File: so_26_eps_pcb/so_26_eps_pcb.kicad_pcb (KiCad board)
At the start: 4 copper layers, 90.2 x 95.9 mm, 47 parts, among them J1 Conn_02x12_Odd_Even, J3 Conn_01x02, SW1 SW_SPDT, U1 LM22679TJ-ADJ/NOPB, U2 LM22679TJ-ADJ/NOPB

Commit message: Started the 3V3 reg
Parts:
- moved D1 128.4 mm to (72.5, 88.1), turned to 180 degrees
- moved L1 108.2 mm to (82.7, 94.2)
- moved R3 108.0 mm to (97.8, 77.8), turned to -90 degrees
- moved R7 107.2 mm to (104.4, 81.1), turned to -90 degrees
- moved C13 101.0 mm to (90.4, 95.4), turned to -90 degrees
- moved R5 100.9 mm to (103.4, 77.0), turned to 180 degrees
- moved C17 99.9 mm to (102.6, 85.9), turned to 180 degrees
- moved C15 98.4 mm to (102.6, 88.7), turned to 180 degrees
- moved C11 96.2 mm to (98.0, 95.4), turned to -90 degrees
- moved C10 76.4 mm to (120.4, 78.8)
- moved C7 1.70 mm to (100.1, 78.6), turned to 90 degrees
- moved R8 1.29 mm to (114.0, 55.9)
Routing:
- net Net-(D2-K): track 29.3 -> 3.84 mm
- net REG_+3V3: track 0.00 -> 22.1 mm
- net Net-(U1-FB): track 0.00 -> 10.0 mm
- net Net-(U1-IADJ): track 0.00 -> 8.15 mm
- net Net-(U1-SS): track 0.00 -> 3.51 mm
- net Net-(U2-FB): track 12.0 -> 13.3 mm
- added copper zone on B.Cu, net REG_+3V3

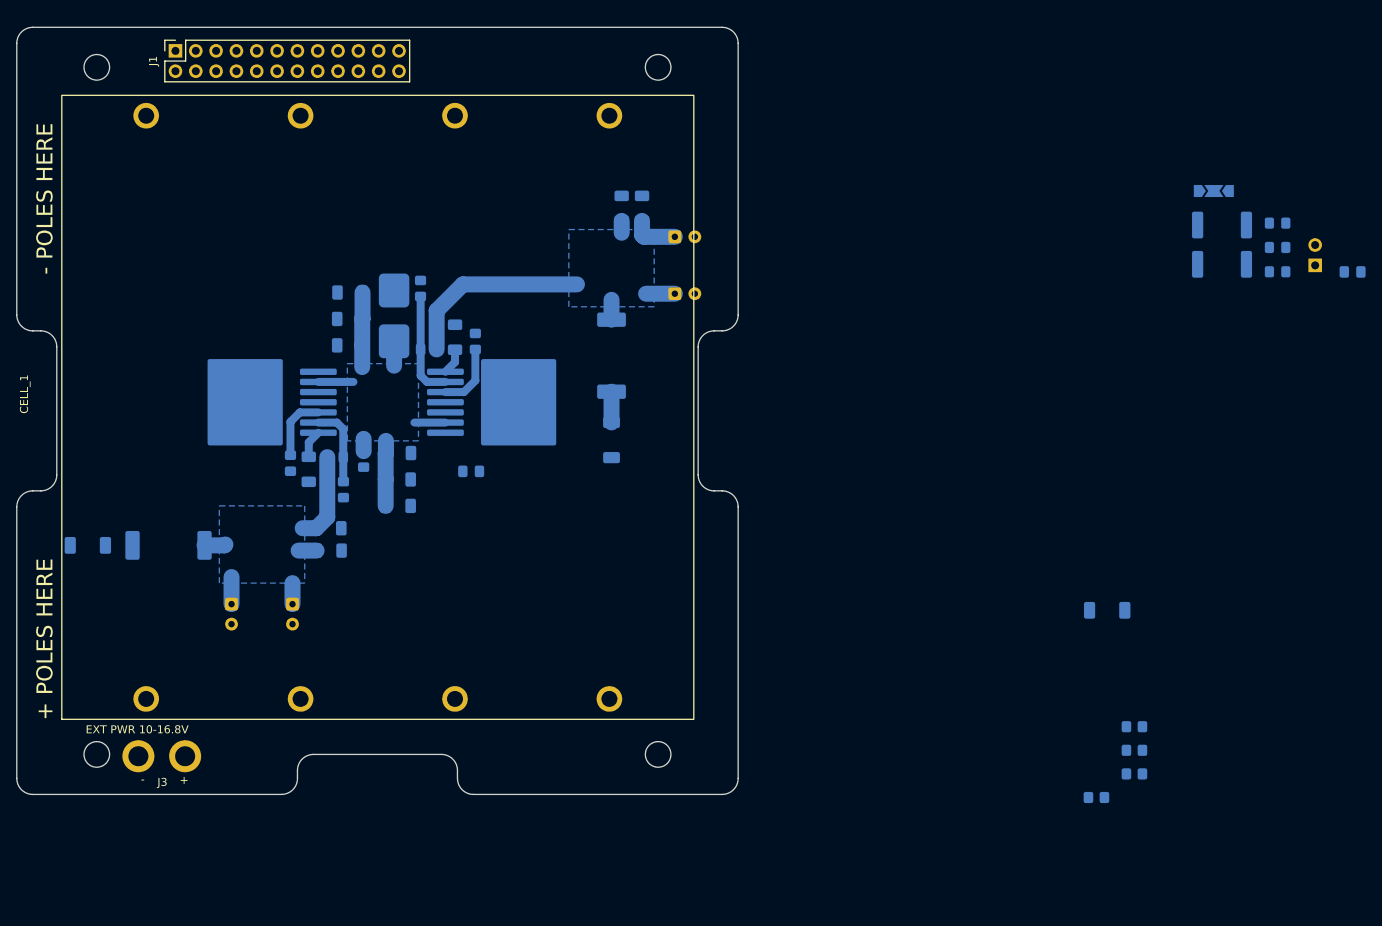
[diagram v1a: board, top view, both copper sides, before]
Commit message: Finished the 3V3 reg
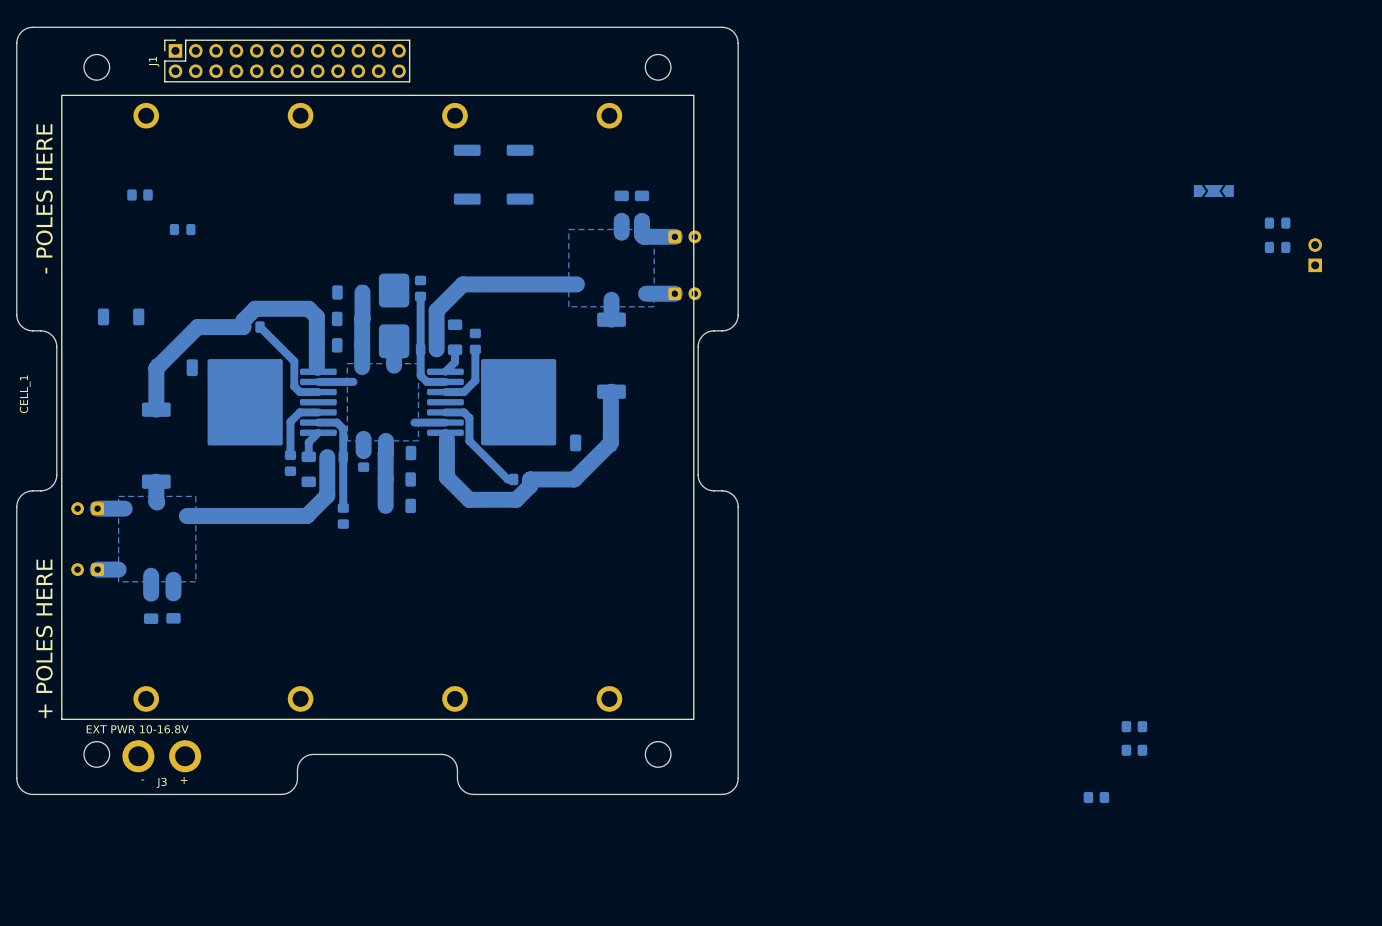
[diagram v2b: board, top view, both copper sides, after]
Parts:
- moved R11 143.8 mm to (79.0, 44.3)
- moved C9 137.8 mm to (92.9, 60.8), turned to 180 degrees
- moved D4 137.0 mm to (84.3, 48.6)
- moved D3 128.6 mm to (76.6, 59.5)
- moved R10 94.6 mm to (119.9, 41.7), turned to 90 degrees
- moved R9 88.5 mm to (126.5, 41.7), turned to 90 degrees
- moved C11 24.7 mm to (73.7, 91.1), turned to 180 degrees
- moved D1 24.7 mm to (83.3, 65.9), turned to 0 degrees
- moved C15 23.3 mm to (80.4, 95.7), turned to 90 degrees
- moved C17 21.7 mm to (83.2, 95.6), turned to 90 degrees
- moved C13 20.6 mm to (73.7, 83.5), turned to 180 degrees
- moved L1 20.0 mm to (74.9, 75.7), turned to -90 degrees
- moved C10 6.43 mm to (126.7, 79.8)
- moved R7 3.30 mm to (104.4, 84.4)
- moved D2 2.31 mm to (135.6, 75.3), turned to 180 degrees
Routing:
- net Net-(D1-K): track 0.00 -> 36.1 mm
- net Net-(D2-K): track 3.84 -> 37.2 mm
- net REG_+3V3: track 22.1 -> 36.0 mm
- net Net-(U2-BOOT): track 0.00 -> 13.7 mm
- net Net-(U1-BOOT): track 0.00 -> 12.5 mm
- net Net-(U1-FB): track 10.0 -> 13.3 mm

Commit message: Uptaded switch footprints
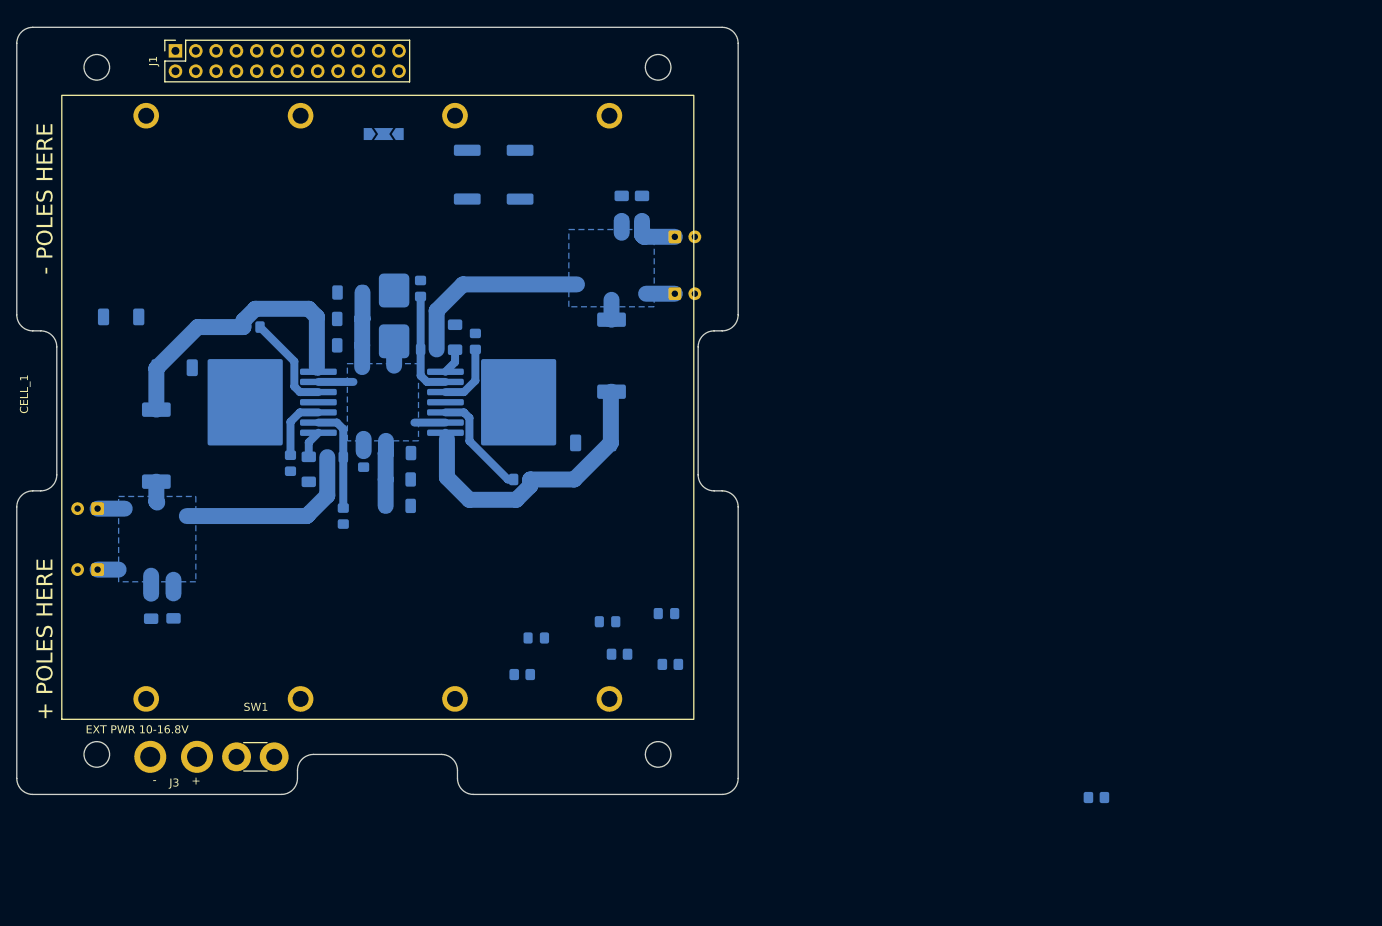
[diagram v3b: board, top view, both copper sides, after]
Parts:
- SW1: footprint Connector_PinSocket_2.54mm:PinSocket_1x02_P2.54mm_Vertical -> Myfootprints:finalswitchfinal; moved to F.Cu
- moved SW1 143.7 mm to (93.5, 108.8)
- moved JP1 104.0 mm to (109.4, 36.6)
- moved D5 95.9 mm to (137.4, 97.6)
- moved D6 90.7 mm to (144.8, 96.6)
- moved R11 76.7 mm to (126.8, 104.2)
- moved D4 67.5 mm to (128.5, 99.6)
- moved R12 65.5 mm to (138.9, 101.7)
- moved R13 58.5 mm to (145.3, 102.9)
- moved J3 1.49 mm to (83.1, 121.0)
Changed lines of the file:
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@@
 		)
 	)
+	(footprint "Myfootprints:finalswitchfinal"
+		(layer "F.Cu")
+		(at 93.472 108.781)
+		(property "Reference" "SW1"
+			(at 0 -0.5 0)
+			(unlocked yes)
+			(layer "F.SilkS")
+			(effects
+				(font
+					(size 1 1)
+					(thickness 0.1)
+				)
+			)
+		)
+		(property "Value" "SW_SPDT"
+			(at 0 1 0)
+			(unlocked yes)
+			(layer "F.Fab")
+			(effects
+				(font
+					(size 1 1)
+					(thickness 0.15)
+				)
+			)
+		)
+		(property "Datasheet" "~"
+			(at 0 0 0)
+			(unlocked yes)
+			(layer "F.Fab")
+			(hide yes)
+			(effects
+				(font
+					(size 1 1)
+					(thickness 0.15)
+				)
+			)
+		)
+		(property "Description" "Switch, single pole double throw"
+			(at 0 0 0)
+			(unlocked yes)
+			(layer "F.Fab")
+			(hide yes)
+			(effects
+				(font
+					(size 1 1)
+					(thickness 0.15)
+				)
+			)
+		)
+		(sheetname "/")
+		(sheetfile "so_26_eps_pcb.kicad_sch")
+		(attr smd)
+		(fp_line
+			(start -1.524 3.937)
+			(end 1.397 3.937)
+			(stroke
+				(width 0.1)
+				(type default)
+			)
+			(layer "F.SilkS")
+		)
+		(fp_line
+			(start -1.524 7.493)
+			(end 1.397 7.493)
+			(stroke
+				(width 0.1)
+				(type default)
+			)
+			(layer "F.SilkS")
+		)
+		(fp_text user "${REFERENCE}"
+			(at 0 2.5 0)
+			(unlocked yes)
+			(layer "F.Fab")
+			(effects
+				(font
+					(size 1 1)
+					(thickness 0.15)
+				)
+			)
+		)
+		(pad "1" thru_hole circle
+			(at -2.424 5.715 90)
+			(size 3.61 3.61)
+			(drill 2)
+			(layers "*.Cu" "*.Mask")
+			(remove_unused_layers no)
+			(net 28 "Net-(J3-Pin_1)")
+			(pinfunction "A")
+			(pintype "passive")
+		)
+		(pad "2" thru_hole circle
+			(at 2.286 5.715)
+			(size 3.61 3.61)
+			(drill 2)
+			(layers "*.Cu" "*.Mask")
+			(remove_unused_layers no)
+			(net 27 "Net-(SW1-B)")
+			(pinfunction "B")
+			(pintype "passive")
+		)
+		(embedded_fonts no)
+	)
 	(footprint "Myfootprints:01x02_header"
 		(layer "F.Cu")
-		(at 81.574 120.8985 180)
+		(at 83.06 120.973 180)
 		(property "Reference" "J3"
 			(at -0.214 3.2275 0)
@@
 		(embedded_fonts no)
 	)
-	(footprint "Connector_PinSocket_2.54mm:PinSocket_1x02_P2.54mm_Vertical"
-		(layer "B.Cu")
-		(at 225.8755 53.059)
-		(descr "Through hole straight socket strip, 1x02, 2.54mm pitch, single row (from Kicad 4.0.7), script generated")
-		(tags "Through hole socket strip THT 1x02 2.54mm single row")
-		(property "Reference" "SW1"
-			(at 0 2.77 180)
-			(layer "B.SilkS")
-			(effects
-				(font
-					(size 1 1)
-					(thickness 0.15)
-				)
-				(justify mirror)
-			)
-		)
-		(property "Value" "SW_SPDT"
-			(at 0 -5.31 180)
-			(layer "B.Fab")
-			(effects
-				(font
-					(size 1 1)
-					(thickness 0.15)
-				)
-				(justify mirror)
-			)
-		)
-		(property "Datasheet" "~"
-			(at 0 0 180)
-			(layer "B.Fab")
-			(hide yes)
-			(effects
-				(font
-					(size 1.27 1.27)
-					(thickness 0.15)
-				)
-				(justify mirror)
-			)
-		)
-		(property "Description" "Switch, single pole double throw"
-			(at 0 0 180)
-			(layer "B.Fab")
-			(hide yes)
-			(effects
-				(font
-					(size 1.27 1.27)
-					(thickness 0.15)
-				)
-				(justify mirror)
-			)
-		)
-		(sheetname "/")
-		(sheetfile "so_26_eps_pcb.kicad_sch")
-		(attr through_hole)
-		(fp_line
-			(start -1.33 -3.87)
-			(end 1.33 -3.87)
-			(stroke
-				(width 0.12)
-				(type solid)
-			)
-			(layer "B.SilkS")
-		)
-		(fp_line
-			(start -1.33 -1.27)
-			(end -1.33 -3.87)
-			(stroke
-				(width 0.12)
-				(type solid)
-			)
-			(layer "B.SilkS")
-		)
-		(fp_line
-			(start -1.33 -1.27)
-			(end 1.33 -1.27)
-			(stroke
-				(width 0.12)
-				(type solid)
-			)
-			(layer "B.SilkS")
-		)
-		(fp_line
-			(start 0 1.33)
-			(end 1.33 1.33)
-			(stroke
-				(width 0.12)
-				(type solid)
-			)
-			(layer "B.SilkS")
-		)
-		(fp_line
-			(start 1.33 -1.27)
-			(end 1.33 -3.87)
-			(stroke
-				(width 0.12)
-				(type solid)
-			)
-			(layer "B.SilkS")
-		)
-		(fp_line
-			(start 1.33 1.33)
-			(end 1.33 0)
-			(stroke
-				(width 0.12)
-				(type solid)
-			)
-			(layer "B.SilkS")
-		)
-		(fp_line
-			(start -1.8 -4.3)
-			(end -1.8 1.8)
-			(stroke
-				(width 0.05)
-				(type solid)
-			)
-			(layer "B.CrtYd")
-		)
-		(fp_line
-			(start -1.8 1.8)
-			(end 1.75 1.8)
-			(stroke
-				(width 0.05)
-				(type solid)
-			)
-			(layer "B.CrtYd")
-		)
-		(fp_line
-			(start 1.75 -4.3)
-			(end -1.8 -4.3)
-			(stroke
-				(width 0.05)
-				(type solid)
-			)
-			(layer "B.CrtYd")
-		)
-		(fp_line
-			(start 1.75 1.8)
-			(end 1.75 -4.3)
-			(stroke
-				(width 0.05)
-				(type solid)
-			)
-			(layer "B.CrtYd")
-		)
-		(fp_line
-			(start -1.27 -3.81)
-			(end -1.27 1.27)
-			(stroke
-				(width 0.1)
-				(type solid)
-			)
-			(layer "B.Fab")
-		)
-		(fp_line
-			(start -1.27 1.27)
-			(end 0.635 1.27)
-			(stroke
-				(width 0.1)
-				(type solid)
-			)
-			(layer "B.Fab")
-		)
-		(fp_line
-			(start 0.635 1.27)
-			(end 1.27 0.635)
-			(stroke
-				(width 0.1)
-				(type solid)
-			)
-			(layer "B.Fab")
-		)
-		(fp_line
-			(start 1.27 -3.81)
-			(end -1.27 -3.81)
-			(stroke
-				(width 0.1)
-				(type solid)
-			)
-			(layer "B.Fab")
-		)
-		(fp_line
-			(start 1.27 0.635)
-			(end 1.27 -3.81)
-			(stroke
-				(width 0.1)
-				(type solid)
-			)
-			(layer "B.Fab")
-		)
-		(fp_text user "${REFERENCE}"
-			(at 0 -1.27 90)
-			(layer "B.Fab")
-			(effects
-				(font
-					(size 1 1)
-					(thickness 0.15)
-				)
-				(justify mirror)
-			)
-		)
-		(pad "1" thru_hole rect
-			(at 0 0)
-			(size 1.7 1.7)
-			(drill 1)
-			(layers "*.Cu" "*.Mask")
-			(remove_unused_layers no)
-			(net 28 "Net-(J3-Pin_1)")
-			(pinfunction "A")
-			(pintype "passive")
-		)
-		(pad "2" thru_hole circle
-			(at 0 -2.54)
-			(size 1.7 1.7)
-			(drill 1)
-			(layers "*.Cu" "*.Mask")
-			(remove_unused_layers no)
-			(net 27 "Net-(SW1-B)")
-			(pinfunction "B")
-			(pintype "passive")
-		)
-		(embedded_fonts no)
-		(model "${KICAD9_3DMODEL_DIR}/Connector_PinSocket_2.54mm.3dshapes/PinSocket_1x02_P2.54mm_Vertical.step"
-			(offset
-				(xyz 0 0 0)
-			)
-			(scale
-				(xyz 1 1 1)
-			)
-			(rotate
-				(xyz 0 0 0)
-			)
-		)
-	)
 	(footprint "Capacitor_SMD:C_1206_3216Metric_Pad1.33x1.80mm_HandSolder"
 		(layer "B.Cu")
@@
 	(footprint "LED_SMD:LED_0805_2012Metric_Pad1.15x1.40mm_HandSolder"
 		(layer "B.Cu")
-		(at 221.1805 50.824)
+		(at 137.423 97.605)
 		(descr "LED SMD 0805 (2012 Metric), square (rectangular) end terminal, IPC-7351 nominal, (Body size source: https://docs.google.com/spreadsheets/d/1BsfQQcO9C6DZCsRaXUlFlo91Tg2WpOkGARC1WS5S8t0/edit?usp=sharing), generated with kicad-footprint-generator")
 		(tags "LED handsolder")
@@
 	(footprint "Resistor_SMD:R_0805_2012Metric_Pad1.20x1.40mm_HandSolder"
 		(layer "B.Cu")
-		(at 78.978 44.265)
+		(at 126.762 104.209)
 		(descr "Resistor SMD 0805 (2012 Metric), square (rectangular) end terminal, IPC-7351 nominal with elongated pad for handsoldering. (Body size source: IPC-SM-782 page 72, https://www.pcb-3d.com/wordpress/wp-content/uploads/ipc-sm-782a_amendment_1_and_2.pdf), generated with kicad-footprint-generator")
 		(tags "resistor handsolder")
@@
 	(footprint "Jumper:SolderJumper-3_P2.0mm_Open_TrianglePad1.0x1.5mm_NumberLabels"
 		(layer "B.Cu")
-		(at 213.2155 43.769)
+		(at 109.442 36.645)
 		(descr "SMD Solder Jumper, 1x1.5mm Triangular Pads, 0.3mm gap, open, labeled with numbers")
 		(tags "solder jumper open")
@@
 	(footprint "LED_SMD:LED_0805_2012Metric_Pad1.15x1.40mm_HandSolder"
 		(layer "B.Cu")
-		(at 84.319 48.583)
+		(at 128.515 99.637)
 		(descr "LED SMD 0805 (2012 Metric), square (rectangular) end terminal, IPC-7351 nominal, (Body size source: https://docs.google.com/spreadsheets/d/1BsfQQcO9C6DZCsRaXUlFlo91Tg2WpOkGARC1WS5S8t0/edit?usp=sharing), generated with kicad-footprint-generator")
 		(tags "LED handsolder")
@@
 	(footprint "Resistor_SMD:R_0805_2012Metric_Pad1.20x1.40mm_HandSolder"
 		(layer "B.Cu")
-		(at 203.286 113.679)
+		(at 138.922 101.669)
 		(descr "Resistor SMD 0805 (2012 Metric), square (rectangular) end terminal, IPC-7351 nominal with elongated pad for handsoldering. (Body size source: IPC-SM-782 page 72, https://www.pcb-3d.com/wordpress/wp-content/uploads/ipc-sm-782a_amendment_1_and_2.pdf), generated with kicad-footprint-generator")
 		(tags "resistor handsolder")
@@
 	(footprint "LED_SMD:LED_0805_2012Metric_Pad1.15x1.40mm_HandSolder"
 		(layer "B.Cu")
-		(at 221.1805 47.784)
+		(at 144.789 96.589)
 		(descr "LED SMD 0805 (2012 Metric), square (rectangular) end terminal, IPC-7351 nominal, (Body size source: https://docs.google.com/spreadsheets/d/1BsfQQcO9C6DZCsRaXUlFlo91Tg2WpOkGARC1WS5S8t0/edit?usp=sharing), generated with kicad-footprint-generator")
 		(tags "LED handsolder")
@@
 	(footprint "Resistor_SMD:R_0805_2012Metric_Pad1.20x1.40mm_HandSolder"
 		(layer "B.Cu")
-		(at 203.286 110.729)
+		(at 145.272 102.939)
 		(descr "Resistor SMD 0805 (2012 Metric), square (rectangular) end terminal, IPC-7351 nominal with elongated pad for handsoldering. (Body size source: IPC-SM-782 page 72, https://www.pcb-3d.com/wordpress/wp-content/uploads/ipc-sm-782a_amendment_1_and_2.pdf), generated with kicad-footprint-generator")
 		(tags "resistor handsolder")

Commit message: Traced and placed the last components
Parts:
- moved R2 109.0 mm to (124.1, 39.9), turned to 180 degrees
- moved R1 43.5 mm to (129.3, 39.9), turned to 180 degrees
- moved R9 42.6 mm to (83.9, 42.9), turned to -90 degrees
- moved D3 33.6 mm to (105.5, 42.4), turned to 180 degrees
- moved R10 29.4 mm to (90.6, 42.9), turned to -90 degrees
- moved JP1 17.3 mm to (126.7, 37.0)
- moved R11 16.4 mm to (143.0, 102.0)
- moved D4 14.7 mm to (143.0, 97.0)
- moved R13 8.19 mm to (137.1, 101.9)
- moved R12 7.77 mm to (131.2, 101.9)
- moved D6 7.63 mm to (137.2, 96.8)
- moved D5 6.29 mm to (131.2, 96.8)
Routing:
- net +10V: track 0.00 -> 107.9 mm, vias 0 -> 2
- net +3V3: track 0.00 -> 95.8 mm, vias 0 -> 2
- net +10V_ALT: track 0.00 -> 90.0 mm, vias 0 -> 2
- net REG_+3V3: track 36.0 -> 110.0 mm, vias 0 -> 1
- net REG_+10V: track 37.3 -> 89.3 mm
- net VBAT: track 30.3 -> 62.2 mm, vias 0 -> 2
- net /VBAT_0: track 0.00 -> 22.7 mm
- net /VBAT_1: track 0.00 -> 21.8 mm
- net Net-(JP1-C): track 0.00 -> 9.12 mm
- net Net-(D6-K): track 0.00 -> 5.08 mm
- net Net-(D5-K): track 0.00 -> 5.08 mm
- net Net-(D4-K): track 0.00 -> 5.08 mm
